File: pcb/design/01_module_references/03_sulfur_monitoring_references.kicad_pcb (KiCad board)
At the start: 2 copper layers, 41 parts, among them U1 SPI SD-CARD, U2 Anemometer, U3 Wind Direction, U4 Heltec WSL V3 JP

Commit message: edit some footprint
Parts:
- removed D1, D2: LED, LED_THT:LED_D5.0mm
- removed I1: INA219, Custom Board:INA219
- removed I2: TB600B SO2, Custom Board:TB600B
- removed I3: TB600C H2S, Custom Board:TB600C
- removed I4: SSD1306​, Custom Board:SSD1306 On-board
- removed I5, I7: GPS, Custom Board:GPS
- removed I6: DS3231​, Custom Board:DS3231
- removed the REF** at (252.8, 294.1)
- removed U1: SPI SD-CARD, Custom Board:SPI SD Card
- removed U2: Anemometer, Custom Board:Anemometer
- removed U3: Wind Direction, Custom Board:Wind Direction
- removed U4: Heltec WSL V3 JP, Custom Board:HELTEC WSL V3 JP
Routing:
- net Net-(D2-A): track 43.8 -> 0.00 mm
- net Net-(D1-A): track 11.2 -> 0.00 mm
- net Net-(D1-K): track 8.67 -> 0.00 mm
- net Net-(D2-K): track 5.08 -> 0.00 mm
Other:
- board text removed: "- ANEMO DAN WIND DIR JADINYA PAKAI JST 4 PIN - PIN 1 (PALING KIRI) JADI GND (KABEL HITAM). PIN 2 MERAH - JSTnya ambil seri ini JST_XH_B4B-XH-A_1x04_P2.50mm_Vertical"
- board text removed: "HELTEC PINNYA KEBALIK ADA YANG TERDUPLIKAT 43 LEBAR PADNYA PAKAI DIAMETER 1.7 mm, HOLE 1 mm"
- board text removed: "INA219 FOOTPRINT AMAN tapi ubah pad ke DIAMETER 1.7 mm, HOLE 1 mm"
- board text removed: "KEBALIK dan ubah ke DIAMETER 1.7 mm"
- board text removed: "REVISI"
- board text removed: "SALAH MODUL ubah pad DIAMETER 1.7 mm, HOLE 1 mm"
- board text removed: "SSD1306 FOOTPRINT AMAN tinggal ubah pad DIAMETER 1.7 mm, HOLE 1 mm"

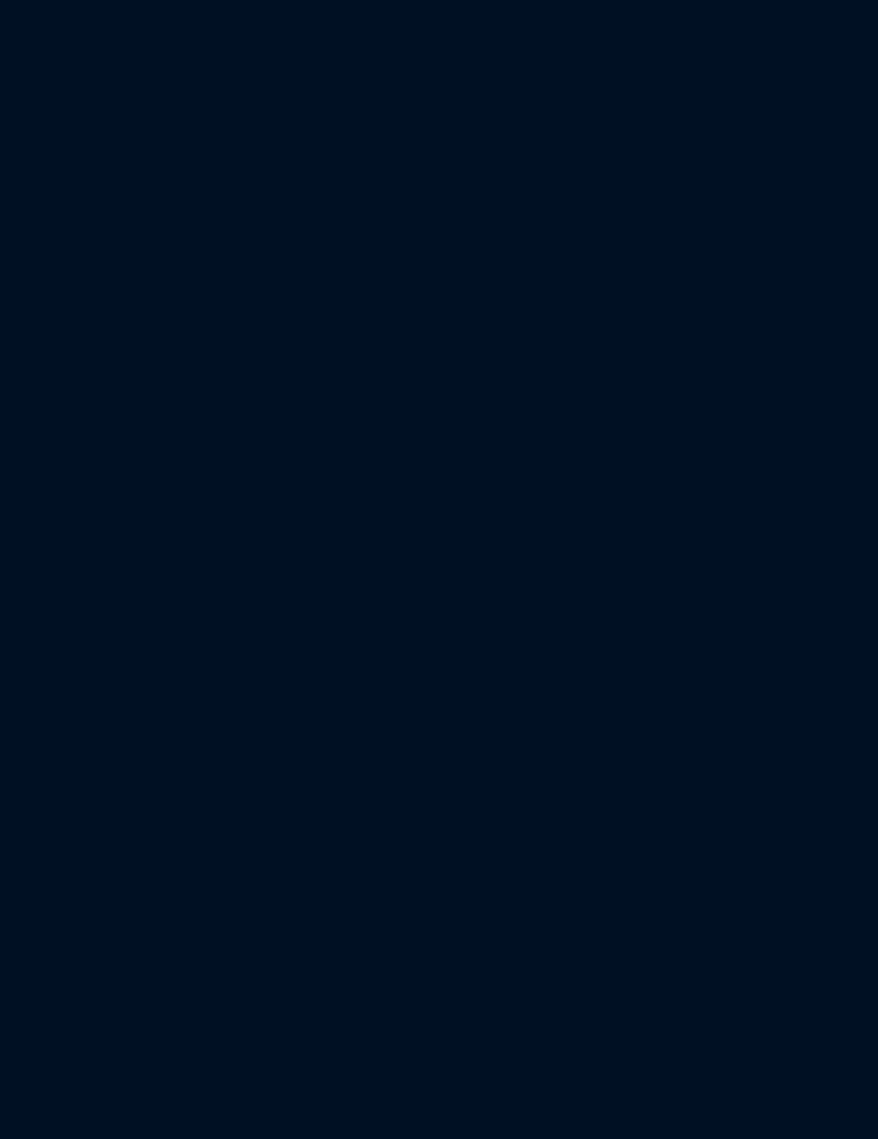
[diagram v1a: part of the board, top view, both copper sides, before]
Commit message: renamed symbol to libraries
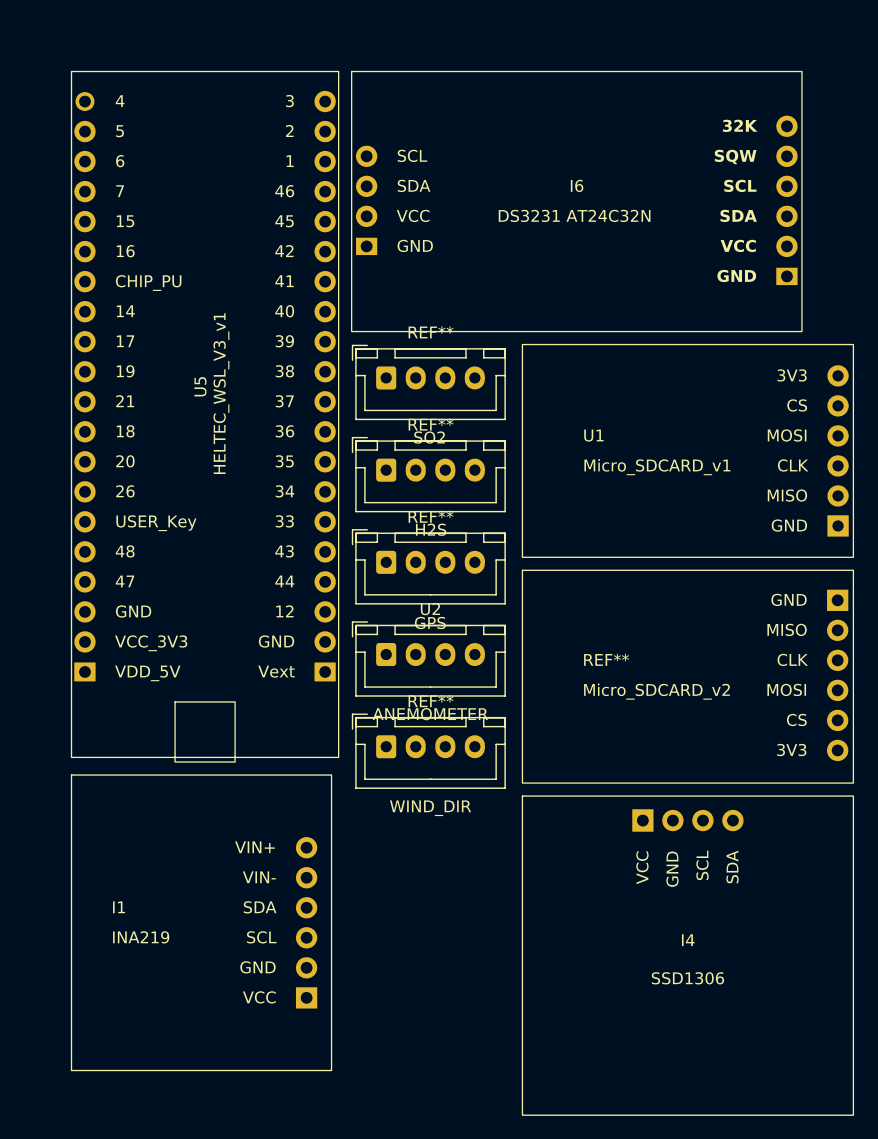
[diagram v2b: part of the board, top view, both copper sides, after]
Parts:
- added I1: INA219, STASRG_myCustom_Footprint:INA219, F.Cu at (240.8, 294.0)
- added I2: TB600B SO2, STASRG_myCustom_Footprint:TB600B_SO2, F.Cu at (260.1, 247.9)
- added I3: TB600C_H2S, STASRG_myCustom_Footprint:TB600C_H2S, F.Cu at (260.2, 255.7)
- added I4: SSD1306​, STASRG_myCustom_Footprint:SSD1306_onBoard, F.Cu at (282.0, 296.8)
- added I5: uBlox_NEO-6M, STASRG_myCustom_Footprint:uBlox_NEO-6M, F.Cu at (260.2, 263.6)
- added I6: DS3231​, STASRG_myCustom_Footprint:DS3231, F.Cu at (272.6, 234.2)
- added U1: Micro_SDCARD_v1, STASRG_myCustom_Footprint:Micro_SDCARD_v1, F.Cu at (282.0, 254.1)
- added U2: Anemometer, STASRG_myCustom_Footprint:STASRG_Anemometer, F.Cu at (260.2, 271.3)
- added U3: Wind_Direction, STASRG_myCustom_Footprint:STASRG_Wind_Dir, F.Cu at (260.2, 279.1)
- added U4: Micro_SDCARD_v2, STASRG_myCustom_Footprint:Micro_SDCARD_v2, F.Cu at (281.9, 273.1)
- added U5: Heltec_WSL_V3, STASRG_myCustom_Footprint:Heltec_WSL_V3_v1, F.Cu at (241.1, 252.4)
- REF** (x5): footprint Connector_PinSocket_2.54mm:PinSocket_1x06_P2.54mm_Vertical -> STASRG_myCustom_Footprint:PinSocket_1x06_P2.54mm_Vertical
- REF** (x6): footprint Connector_PinHeader_2.54mm:PinHeader_1x04_P2.54mm_Vertical -> STASRG_myCustom_Footprint:PinHeader_1x04_P2.54mm_Vertical
- REF** (x8): footprint Connector_PinSocket_2.54mm:PinSocket_1x02_P2.54mm_Vertical -> STASRG_myCustom_Footprint:PinSocket_1x02_P2.54mm_Vertical
- REF** (x5): footprint Connector_JST:JST_XH_B4B-XH-A_1x04_P2.50mm_Vertical -> STASRG_myCustom_Footprint:JST_XH_B4B-XH-A_1x04_P2.50mm_Vertical
- REF** (x2): footprint Connector_PinSocket_2.54mm:PinSocket_1x20_P2.54mm_Vertical -> STASRG_myCustom_Footprint:PinSocket_1x20_P2.54mm_Vertical
- REF**: footprint Connector_PinSocket_2.54mm:PinSocket_1x04_P2.54mm_Vertical -> STASRG_myCustom_Footprint:PinSocket_1x04_P2.54mm_Vertical
